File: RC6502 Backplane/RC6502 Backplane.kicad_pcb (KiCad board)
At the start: 2 copper layers, 99.1 x 99.1 mm, 20 parts, among them J1 RC6502_Backplane, J10 Mounting, J2 Barrel_Jack, J3 RC6502_Backplane, J4 RC6502_Backplane, J5 RC6502_Backplane, J6 RC6502_Backplane, J7 Mounting, J8 Mounting, J9 Mounting, U1 LM7805

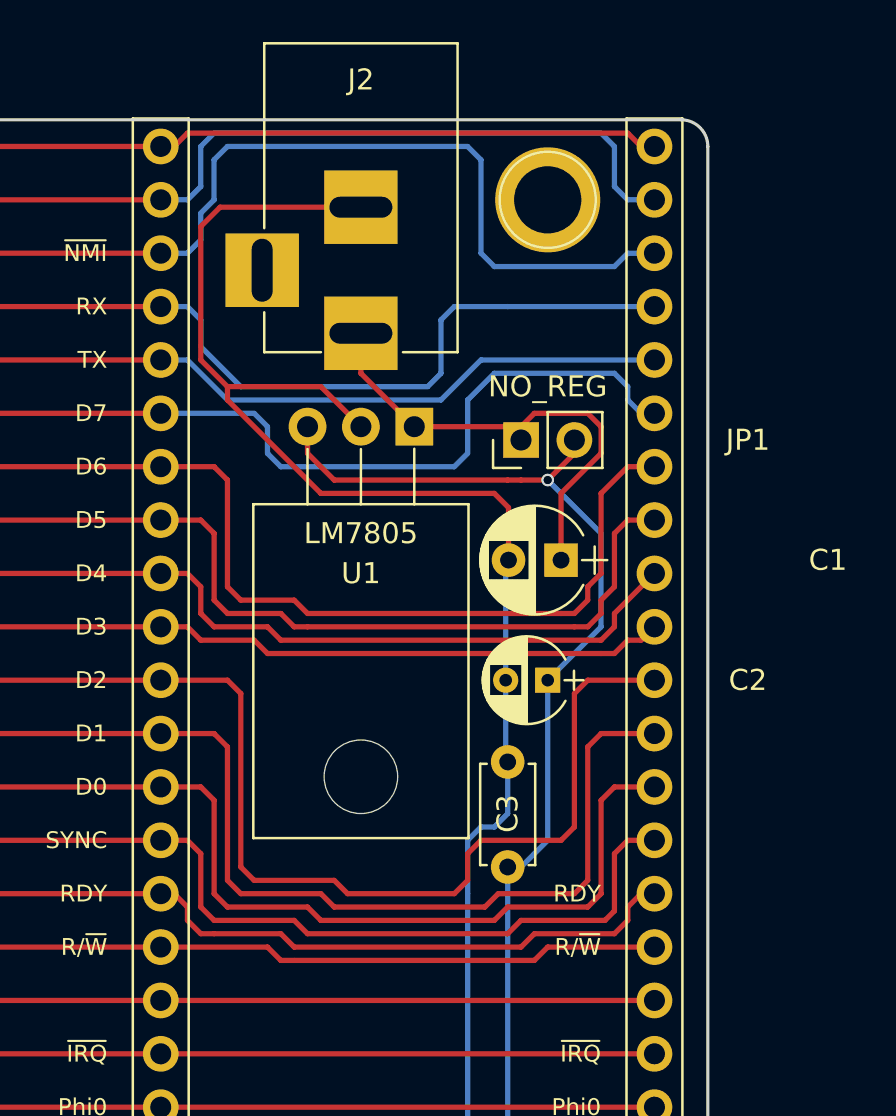
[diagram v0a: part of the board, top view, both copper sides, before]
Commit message: Added bleed LED to backplane
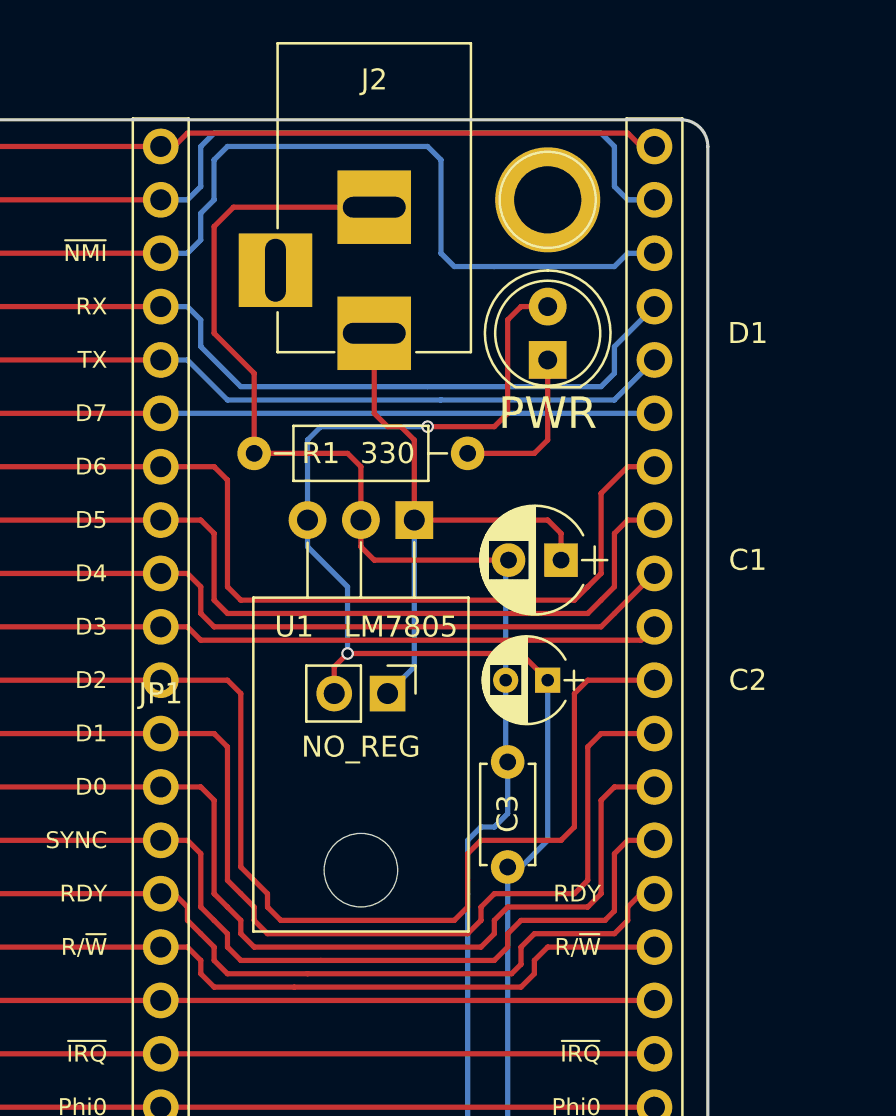
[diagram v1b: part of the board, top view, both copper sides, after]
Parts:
- added D1: PWR_LED, LEDs:LED_D5.0mm, F.Cu at (153.7, 69.8)
- added R1: 330, Resistors_THT:R_Axial_DIN0207_L6.3mm_D2.5mm_P10.16mm_Horizontal, F.Cu at (149.9, 74.3)
- moved JP1 13.6 mm to (146.1, 85.7), turned to 270 degrees
- moved U1 4.44 mm to (147.3, 77.5)
- moved J2 0.63 mm to (145.4, 68.6)
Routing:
- net VCC: track 153.3 -> 165.9 mm, vias 2 -> 3
- net Net-(D1-Pad1): track 0.00 -> 8.52 mm
- net /D7: track 100.3 -> 94.0 mm
- net GND: track 178.8 -> 173.2 mm
- net Net-(C1-Pad1): track 23.0 -> 27.4 mm
- net /D2: track 111.7 -> 113.9 mm
- net /RDY: track 96.8 -> 98.7 mm
- net /D0: track 104.4 -> 106.2 mm
- net /SYNC: track 100.7 -> 102.5 mm
- net /R/~W: track 94.5 -> 96.3 mm
- net /D1: track 108.3 -> 110.1 mm
- net /D6: track 105.3 -> 104.4 mm
- net (no net): track 0.00 -> 0.90 mm
- net /D4: track 97.7 -> 96.8 mm
- net /D5: track 101.9 -> 101.0 mm
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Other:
- board text added: "Center positive 7-12v Center positive 5v (NO_REG)"
- board text added: "PWR"
- board text added: "Revision B"
- board text removed: "Revision A"
